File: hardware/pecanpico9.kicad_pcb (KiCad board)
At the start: 4 copper layers, 29.8 x 33.7 mm, 111 parts, among them IC1 SPV1040T, IC2 TPS62260DRVR, IC3 ADP322ACPZ-115-R7, IC4 Si4063-B1B-FM, IC5 STM32F413xG, IC6 EVA-7M, IC7 PAC1720-1-AIA-TR, IC8 LDLN015PU33R, IC9 BME280, P1 CONN_01X25, P2 CONN_01X10, P3 ZX62-B-5PA(33), P4 IPX 2mm, P5 CONN_01X02, P6 IPX 2mm, Q1 FDN306P, X1 KT2016K26000BCW18ZAS

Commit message: Wiggled parts around
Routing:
- net GND: track 83.9 -> 85.9 mm, vias 74 -> 75
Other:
- net class Default: clearance 0.149 -> 0.15
- rule trace_clearance: 0.149 -> 0.15
- board text added: "GPS"
- board text removed: "+3.3V"
- board text removed: "+ANALOG"
- board text removed: "+CORE"
- board text removed: "CLK CTRL"
- board text removed: "CS"
- board text removed: "IRQ"
- board text removed: "MISO"
- board text removed: "MOSI"
- board text removed: "RES"
- board text removed: "RXD"
- board text removed: "SCK"
- board text removed: "SCL"
- board text removed: "SDA"
- board text removed: "TXD"

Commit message: Wiggled parts around
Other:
- net class Default: clearance 0.15 -> 0.149
- rule trace_clearance: 0.15 -> 0.149
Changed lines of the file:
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@@
     (thickness 1)
     (drawings 30)
-    (tracks 1487)
+    (tracks 1489)
     (zones 0)
     (modules 111)
@@
   (setup
     (last_trace_width 0.2)
-    (trace_clearance 0.15)
+    (trace_clearance 0.149)
     (zone_clearance 0.15)
     (zone_45_only no)
@@
   (net 78 /CAM_PCLK)
   (net_class Default "This is the default net class."
-    (clearance 0.15)
+    (clearance 0.149)
     (trace_width 0.2)
     (via_dia 0.5)
@@
   (via (at 58.35 110.9) (size 0.5) (drill 0.3) (layers F.Cu B.Cu) (net 22))
   (via (at 53.9 111) (size 0.5) (drill 0.3) (layers F.Cu B.Cu) (net 22))
+  (segment (start 71.05 121.65) (end 71.05 121.690002) (width 0.2) (layer B.Cu) (net 23))
+  (segment (start 70.110479 122.149001) (end 69.850999 121.889521) (width 0.2) (layer B.Cu) (net 23))
+  (segment (start 70.249001 117.339521) (end 70.249001 116.860479) (width 0.2) (layer B.Cu) (net 23))
+  (segment (start 71.05 121.690002) (end 70.591001 122.149001) (width 0.2) (layer B.Cu) (net 23))
+  (segment (start 70.591001 122.149001) (end 70.110479 122.149001) (width 0.2) (layer B.Cu) (net 23))
+  (segment (start 69.850999 121.889521) (end 69.850999 121.512477) (width 0.2) (layer B.Cu) (net 23))
+  (segment (start 69.850999 121.512477) (end 68.95199 120.613468) (width 0.2) (layer B.Cu) (net 23))
+  (segment (start 70.249001 116.860479) (end 70.051374 116.662852) (width 0.2) (layer B.Cu) (net 23))
+  (segment (start 68.95199 118.12368) (end 69.476669 117.599001) (width 0.2) (layer B.Cu) (net 23))
+  (segment (start 68.95199 120.613468) (end 68.95199 118.12368) (width 0.2) (layer B.Cu) (net 23))
+  (segment (start 69.476669 117.599001) (end 69.989521 117.599001) (width 0.2) (layer B.Cu) (net 23))
+  (segment (start 69.849384 116.44801) (end 68.830106 116.44801) (width 0.2) (layer B.Cu) (net 23))
+  (segment (start 69.989521 117.599001) (end 70.249001 117.339521) (width 0.2) (layer B.Cu) (net 23))
+  (segment (start 70.051374 116.662852) (end 70.051374 116.65) (width 0.2) (layer B.Cu) (net 23))
+  (segment (start 70.051374 116.65) (end 69.849384 116.44801) (width 0.2) (layer B.Cu) (net 23))
+  (segment (start 68.830106 116.44801) (end 68.083095 115.700999) (width 0.2) (layer B.Cu) (net 23))
+  (segment (start 68.083095 115.700999) (end 67.035907 115.700999) (width 0.2) (layer B.Cu) (net 23))
+  (segment (start 67.035907 115.700999) (end 65.4 114.065092) (width 0.2) (layer B.Cu) (net 23))
+  (segment (start 65.4 114.065092) (end 65.4 113.7) (width 0.2) (layer B.Cu) (net 23))
+  (segment (start 70.951798 121.5) (end 70.851798 121.4) (width 0.2) (layer F.Cu) (net 23))
+  (segment (start 70.851798 121.4) (end 70.75 121.298202) (width 0.2) (layer F.Cu) (net 23))
+  (segment (start 71.05 121.65) (end 71.05 121.598202) (width 0.2) (layer F.Cu) (net 23))
+  (segment (start 71.05 121.598202) (end 70.851798 121.4) (width 0.2) (layer F.Cu) (net 23))
   (segment (start 65.4 113.7) (end 65.4 113.6) (width 0.2) (layer B.Cu) (net 23))
   (segment (start 65.7 109.017838) (end 65.94999 108.767848) (width 0.2) (layer B.Cu) (net 23))
@@
   (segment (start 60.3 113.55) (end 64.3 113.55) (width 0.2) (layer F.Cu) (net 23))
   (segment (start 64.3 113.55) (end 64.30099 113.54901) (width 0.2) (layer F.Cu) (net 23))
-  (segment (start 70.051374 116.662852) (end 70.249001 116.860479) (width 0.2) (layer B.Cu) (net 23))
-  (segment (start 65.4 113.7) (end 65.4 114.065092) (width 0.2) (layer B.Cu) (net 23))
-  (segment (start 69.989521 117.599001) (end 69.476669 117.599001) (width 0.2) (layer B.Cu) (net 23))
-  (segment (start 67.035907 115.700999) (end 68.083095 115.700999) (width 0.2) (layer B.Cu) (net 23))
-  (segment (start 69.849384 116.44801) (end 70.051374 116.65) (width 0.2) (layer B.Cu) (net 23))
-  (segment (start 65.4 114.065092) (end 67.035907 115.700999) (width 0.2) (layer B.Cu) (net 23))
-  (segment (start 68.083095 115.700999) (end 68.830106 116.44801) (width 0.2) (layer B.Cu) (net 23))
-  (segment (start 70.051374 116.65) (end 70.051374 116.662852) (width 0.2) (layer B.Cu) (net 23))
-  (segment (start 68.830106 116.44801) (end 69.849384 116.44801) (width 0.2) (layer B.Cu) (net 23))
-  (segment (start 69.476669 117.599001) (end 68.95199 118.12368) (width 0.2) (layer B.Cu) (net 23))
-  (segment (start 70.249001 116.860479) (end 70.249001 117.339521) (width 0.2) (layer B.Cu) (net 23))
-  (segment (start 70.249001 117.339521) (end 69.989521 117.599001) (width 0.2) (layer B.Cu) (net 23))
-  (segment (start 70.750999 122.149001) (end 71.25 121.65) (width 0.2) (layer B.Cu) (net 23))
-  (segment (start 68.95199 118.12368) (end 68.95199 120.613468) (width 0.2) (layer B.Cu) (net 23))
-  (segment (start 68.95199 120.613468) (end 69.850999 121.512477) (width 0.2) (layer B.Cu) (net 23))
-  (segment (start 69.850999 121.512477) (end 69.850999 121.889521) (width 0.2) (layer B.Cu) (net 23))
-  (segment (start 69.850999 121.889521) (end 70.110479 122.149001) (width 0.2) (layer B.Cu) (net 23))
-  (segment (start 70.110479 122.149001) (end 70.750999 122.149001) (width 0.2) (layer B.Cu) (net 23))
   (segment (start 58.3 114.55) (end 58.3 114.638522) (width 0.2) (layer B.Cu) (net 23))
   (segment (start 58.3 114.638522) (end 57.888511 115.050011) (width 0.2) (layer B.Cu) (net 23))
@@
   (segment (start 72.9 121.5) (end 71.1 121.5) (width 0.2) (layer F.Cu) (net 23))
   (segment (start 71.1 121.5) (end 70.951798 121.5) (width 0.2) (layer F.Cu) (net 23))
-  (segment (start 71.25 121.65) (end 71.1 121.5) (width 0.2) (layer F.Cu) (net 23))
   (segment (start 72.9 121.5) (end 73.2 121.5) (width 0.2) (layer F.Cu) (net 23))
-  (segment (start 70.951798 121.5) (end 70.75 121.298202) (width 0.2) (layer F.Cu) (net 23))
   (segment (start 70.75 120.7) (end 70.75 121.298202) (width 0.2) (layer F.Cu) (net 23))
-  (segment (start 71.101798 121.65) (end 71.25 121.65) (width 0.2) (layer F.Cu) (net 23))
-  (via (at 71.25 121.65) (size 0.5) (drill 0.3) (layers F.Cu B.Cu) (net 23))
+  (via (at 71.05 121.65) (size 0.5) (drill 0.3) (layers F.Cu B.Cu) (net 23))
   (segment (start 58.3 114.25) (end 58.3 114.55) (width 0.2) (layer F.Cu) (net 23))
   (segment (start 65.499001 113.799001) (end 65.4 113.7) (width 0.2) (layer B.Cu) (net 23))

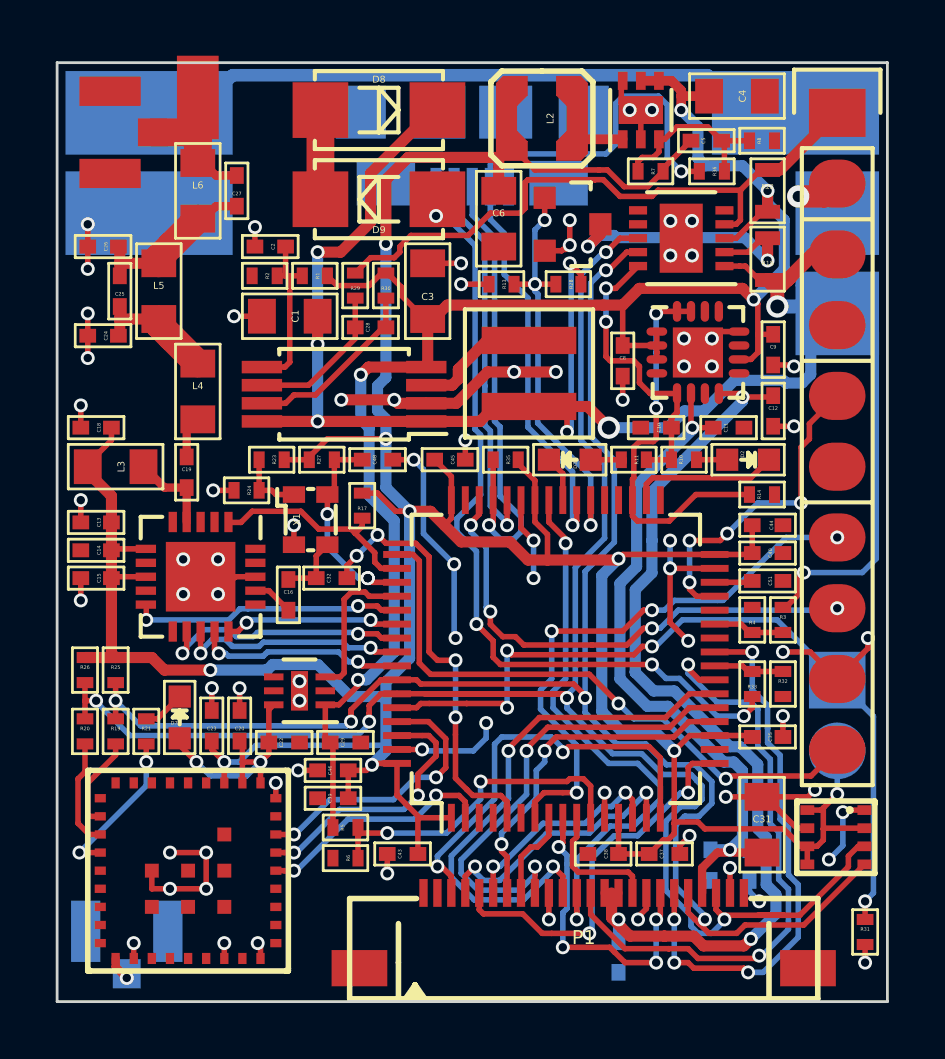
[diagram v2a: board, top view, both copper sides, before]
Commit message: Connected VUSB correctly to PA9
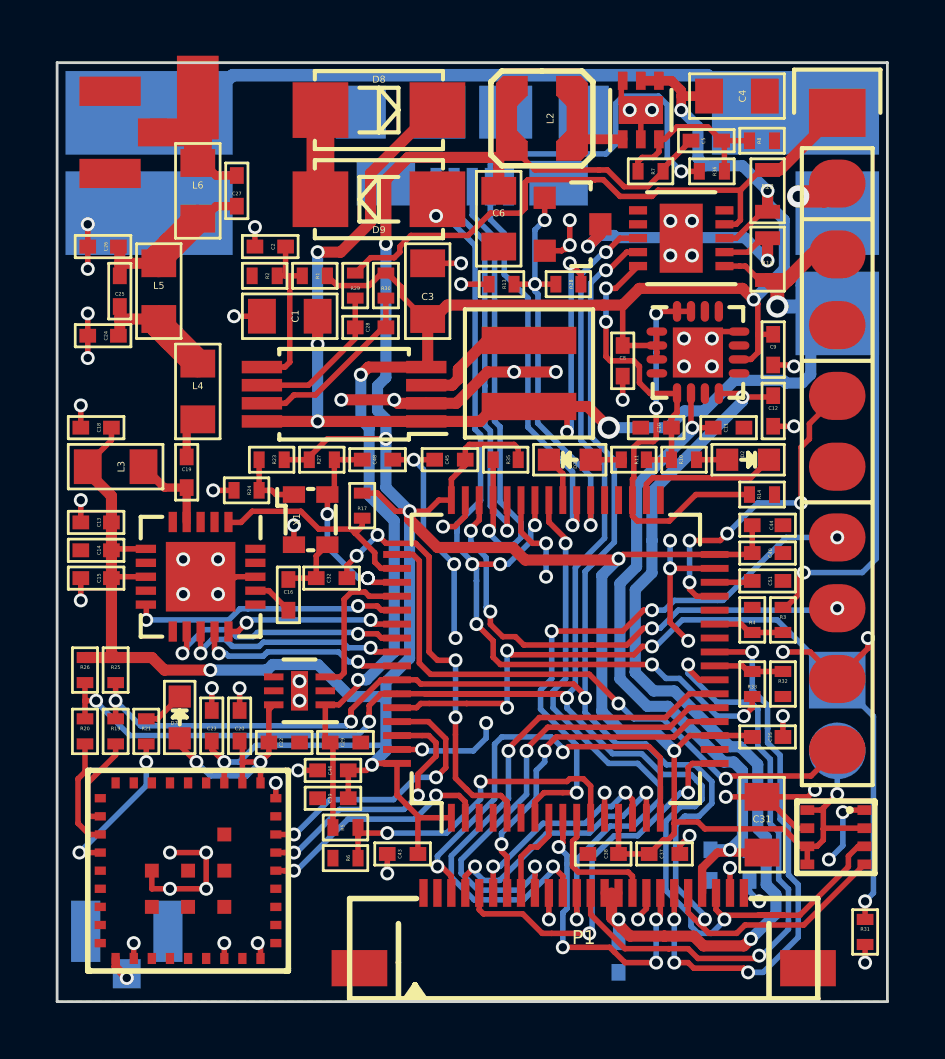
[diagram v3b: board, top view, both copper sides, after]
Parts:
- turned C45 to 0 degrees
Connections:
- IC5 pad 42: +1V8 -> /USB_VUSB
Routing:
- net /USB_VUSB: track 29.4 -> 33.5 mm, vias 4 -> 7
- net GND: track 85.9 -> 87.9 mm
